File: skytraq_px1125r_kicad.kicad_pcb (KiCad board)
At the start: 2 copper layers, 35.5 x 27.6 mm, 11 parts, among them J1 Conn_01x04, J2 SMA, J3 SH_Conn_01x04, J4 Conn_01x04, U1 Skytraq_PX1125R

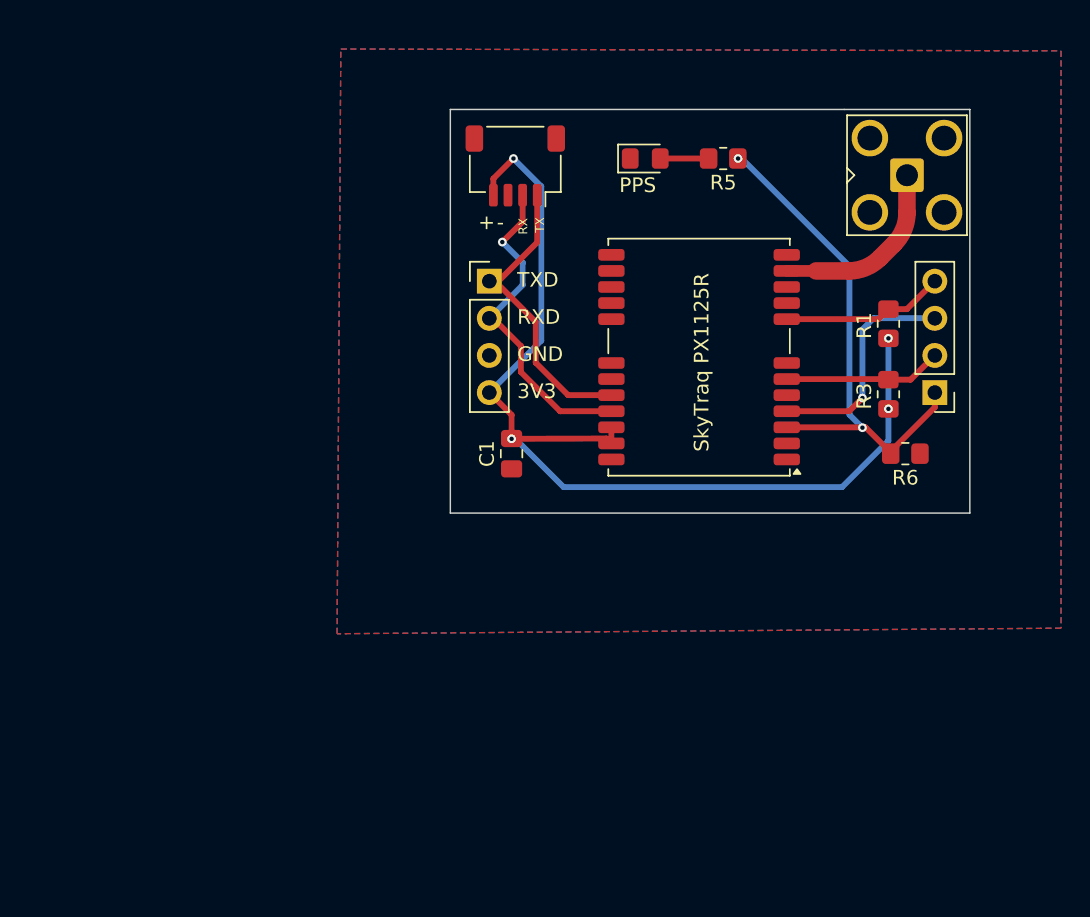
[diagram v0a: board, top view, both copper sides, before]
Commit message: 36x36 flight controller board
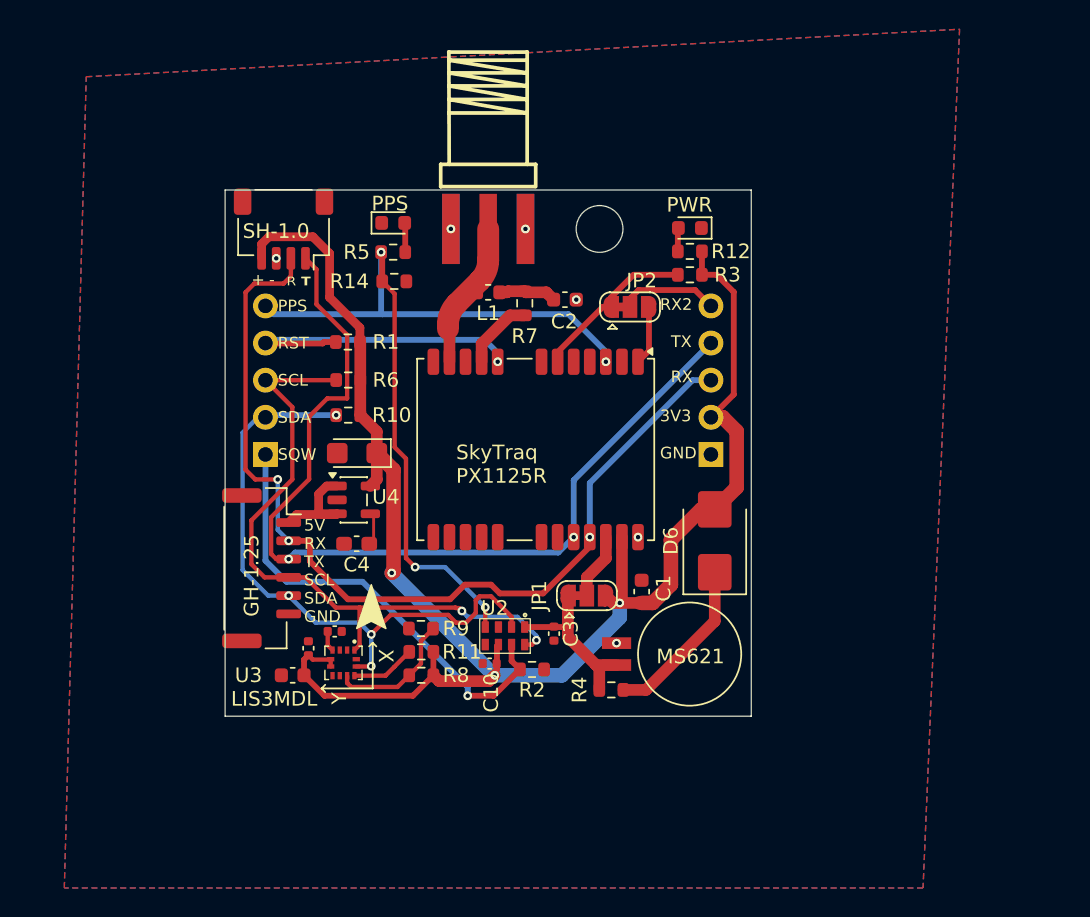
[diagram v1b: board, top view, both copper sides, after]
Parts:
- removed J3: SH_Conn_01x04, Connector_JST:JST_SH_SM04B-SRSS-TB_1x04-1MP_P1.00mm_Horizontal
- added BT1: MS621FE, Battery:BatteryHolder_Seiko_MS621F, F.Cu at (116.8, 71.8)
- added C10: 100nF, Capacitor_SMD:C_0402_1005Metric, F.Cu at (108.1, 72.4)
- added C2: 47pF, Capacitor_SMD:C_0603_1608Metric, F.Cu at (113.2, 47.5)
- added C23: 10uF, Capacitor_SMD:C_0603_1608Metric, F.Cu at (94.6, 73.2)
- added C3: 100nF, Capacitor_SMD:C_0402_1005Metric, F.Cu at (112.5, 70.3)
- added C4: 470pF, Capacitor_SMD:C_0603_1608Metric_Pad1.08x0.95mm_HandSolder, F.Cu at (99.0, 64.2)
- added C5: 2.2uF, Capacitor_Tantalum_SMD:CP_EIA-3216-18_Kemet-A, F.Cu at (99.0, 58.0)
- added C8: 100nF, Capacitor_SMD:C_0402_1005Metric, F.Cu at (95.7, 71.4)
- added C9: 100nF, Capacitor_SMD:C_0402_1005Metric, F.Cu at (97.5, 70.2)
- added D1: BLUE, LED_SMD:LED_0603_1608Metric, F.Cu at (121.8, 42.6)
- added D6: D_Schottky, Diode_SMD:D_SMB, F.Cu at (123.5, 64.0)
- added H1: MountingHole, MountingHole:MountingHole_3.2mm_M3, F.Cu at (115.6, 42.7)
- added J5: Conn_01x05, Connector_PinHeader_2.54mm:PinHeader_1x05_P2.54mm_Horizontal, B.Cu at (92.8, 58.1)
- added J7: Conn_01x05, Connector_PinHeader_2.54mm:PinHeader_1x05_P2.54mm_Horizontal, B.Cu at (123.2, 58.1)
- added JP1: SolderJumper_3_Bridged12, Jumper:SolderJumper-3_P1.3mm_Bridged12_RoundedPad1.0x1.5mm, F.Cu at (114.8, 67.8)
- added JP2: SolderJumper_3_Bridged12, Jumper:SolderJumper-3_P1.3mm_Bridged12_RoundedPad1.0x1.5mm, F.Cu at (117.7, 48.0)
- added L1: 27nH, Inductor_SMD:L_0603_1608Metric, F.Cu at (108.0, 47.0)
- added R10: 10k, Resistor_SMD:R_0603_1608Metric, F.Cu at (98.4, 55.4)
- added R11: 10k, Resistor_SMD:R_0603_1608Metric, F.Cu at (103.4, 71.6)
- added R12: 1k, Resistor_SMD:R_0603_1608Metric, F.Cu at (121.8, 44.2)
- added R14: 10k, Resistor_SMD:R_0603_1608Metric, F.Cu at (101.6, 46.2)
- added R2: 10k, Resistor_SMD:R_0603_1608Metric, F.Cu at (111.0, 72.8)
- added R4: 1k, Resistor_SMD:R_0603_1608Metric, F.Cu at (116.4, 74.2)
- added R7: 10, Resistor_SMD:R_0603_1608Metric, F.Cu at (110.5, 47.8)
- added R8: 0, Resistor_SMD:R_0603_1608Metric, F.Cu at (103.4, 73.2)
- added R9: 0, Resistor_SMD:R_0603_1608Metric, F.Cu at (103.4, 70.0)
- added U2: RV-3032, MyFootprints:RV-3032, F.Cu at (109.2, 70.5)
- added U3: LIS3MDL, footprint_JLCPCB:LGA-12_L2.0-W2.0-P0.50-BL, F.Cu at (98.1, 72.4)
- added U4: MIC5219-3.3YM5, Package_TO_SOT_SMD:SOT-23-5, F.Cu at (98.8, 61.2)
- C1: footprint Capacitor_SMD:C_0805_2012Metric_Pad1.18x1.45mm_HandSolder -> Capacitor_SMD:C_0603_1608Metric
- D2: footprint LED_SMD:LED_0805_2012Metric_Pad1.15x1.40mm_HandSolder -> LED_SMD:LED_0603_1608Metric
- J1: value Conn_01x04 -> JST_GH_1.25_6P; footprint Connector_PinHeader_2.54mm:PinHeader_1x04_P2.54mm_Vertical -> Connector_JST:JST_GH_SM06B-GHS-TB_1x06-1MP_P1.25mm_Horizontal
- J2: footprint Connector_Coaxial:SMA_Amphenol_901-143_Horizontal -> footprint_JLCPCB:SMA-SMD_BWSMA-KE-P001
- J4: value Conn_01x04 -> JST_SH_1.00_4P; footprint Connector_PinHeader_2.54mm:PinHeader_1x04_P2.54mm_Vertical -> Connector_JST:JST_SH_SM04B-SRSS-TB_1x04-1MP_P1.00mm_Horizontal
- R1, R3, R6: footprint Resistor_SMD:R_0805_2012Metric_Pad1.20x1.40mm_HandSolder -> Resistor_SMD:R_0603_1608Metric
- R5: value 3k3 -> 1k; footprint Resistor_SMD:R_0805_2012Metric_Pad1.20x1.40mm_HandSolder -> Resistor_SMD:R_0603_1608Metric
- moved J1 47.6 mm to (92.5, 65.9), turned to -90 degrees
- moved R6 38.4 mm to (98.4, 53.0)
- moved R1 37.0 mm to (98.4, 50.4), turned to 180 degrees
- moved J2 28.9 mm to (108.0, 42.7), turned to 90 degrees
- moved R5 23.5 mm to (101.5, 44.2), turned to 0 degrees
- moved D2 17.8 mm to (101.5, 42.2)
- moved R3 15.9 mm to (121.8, 45.8), turned to 0 degrees
- moved J4 14.5 mm to (94.0, 42.7), turned to 180 degrees
- moved C1 13.0 mm to (118.5, 67.5)
- moved U1 12.8 mm to (111.2, 57.8), turned to -90 degrees
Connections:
- C1 pad 1: GND -> +3V3
- C1 pad 2: +3V3 -> GND
- J1 pad 1: GPS_PPS -> /+5V
- J1 pad 2: GPS_RXD2 -> GPS_RX
- J1 pad 3: GPS_EXTINT -> GPS_TX
- J1 pad 4: GPS_RST -> SCL
- J4 pad 1: GPS_TXD -> GPS_TX
- J4 pad 2: GPS_RXD -> GPS_RX
- R1 pad 1: GPS_RST -> +3V3
- R1 pad 2: +3V3 -> GPS_RST
- R3 pad 1: GPS_RXD2 -> Net-(JP2-A)
- R6 pad 1: GND -> +3V3
- R6 pad 2: GPS_PPS -> SCL
- U1 pad 1: unconnected-(U1-BOOT_SEL-Pad1) -> Net-(JP2-B)
- U1 pad 20: GPS_TXD -> GPS_TX
- U1 pad 21: GPS_RXD -> GPS_RX
- U1 pad 22: +3V3 -> Net-(JP1-C)
- U1 pad 4: GPS_EXTINT -> unconnected-(U1-ODO-Pad4)
- U1 pad 6: GPS_RXD2 -> Net-(JP2-A)
- U1 pad 9: unconnected-(U1-SPI_CSN-Pad9) -> Net-(U1-SPI_CSN)
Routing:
- net GPS_RX: track 0.00 -> 64.5 mm, vias 0 -> 3
- net GPS_TX: track 0.00 -> 63.0 mm, vias 0 -> 2
- net +3V3: track 68.7 -> 113.9 mm, vias 4 -> 3
- net SCL: track 0.00 -> 45.2 mm, vias 0 -> 2
- net SDA: track 0.00 -> 43.0 mm, vias 0 -> 4
- net RTC_CLK: track 0.00 -> 31.5 mm, vias 0 -> 1
- net GPS_PPS: track 35.3 -> 59.4 mm, vias 2 -> 4
- net GPS_RXD: track 22.6 -> 0.00 mm, vias 1 -> 0
- net GPS_TXD: track 20.8 -> 0.00 mm
- net GPS_EXTINT: track 15.5 -> 0.00 mm, vias 1 -> 0
- net /VBAT: track 0.00 -> 11.7 mm
- net Net-(D6-K): track 0.00 -> 11.5 mm
- net Net-(JP2-A): track 0.00 -> 11.5 mm
- net GPS_RXD2: track 10.8 -> 0.00 mm
- net GPS_RST: track 11.2 -> 21.8 mm, vias 0 -> 1
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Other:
- board size 35.5 x 27.6 mm -> 36 x 36 mm
- board text added: "5V"
- board text added: "GH-1.25"
- board text added: "LIS3MDL"
- board text added: "MS621"
- board text added: "PWR"
- board text added: "R"
- board text added: "RX2"
- board text added: "SCL"
- board text added: "SDA"
- board text added: "SH-1.0"
- board text added: "SQW"
- board text added: "T"
- board text removed: "ODO"
- board text removed: "RXD"
- board text removed: "RXD2"
- board text removed: "TXD"

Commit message: with px1105 unfinished
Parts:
- removed C4: 470pF, Capacitor_SMD:C_0603_1608Metric_Pad1.08x0.95mm_HandSolder
- removed C5: 2.2uF, Capacitor_Tantalum_SMD:CP_EIA-3216-18_Kemet-A
- removed J4: JST_SH_1.00_4P, Connector_JST:JST_SH_SM04B-SRSS-TB_1x04-1MP_P1.00mm_Horizontal
- removed U4: MIC5219-3.3YM5, Package_TO_SOT_SMD:SOT-23-5
- added C6: 22uF, Capacitor_Tantalum_SMD:CP_EIA-3216-18_Kemet-A, F.Cu at (79.9, 62.1)
- added C7: 10uF, Capacitor_SMD:C_0603_1608Metric, F.Cu at (84.7, 61.8)
- added U5: ~, MyFootprints:skytraq_px1105, B.Cu at (111.2, 53.5)
- added U6: AMS1117-3.3, Package_TO_SOT_SMD:SOT-223-3_TabPin2, F.Cu at (81.9, 56.4)
- D6: footprint Diode_SMD:D_SMB -> Diode_SMD:D_SOD-323
- J2: footprint footprint_JLCPCB:SMA-SMD_BWSMA-KE-P001 -> footprint_JLCPCB:SMA-SMD_BWSMA-KE-P001_Symmetric
- J5: value Conn_01x05 -> Conn_01x04; footprint Connector_PinHeader_2.54mm:PinHeader_1x05_P2.54mm_Horizontal -> Connector_PinSocket_2.54mm:PinSocket_1x04_P2.54mm_Vertical
- J7: value Conn_01x05 -> Conn_01x06; footprint Connector_PinHeader_2.54mm:PinHeader_1x05_P2.54mm_Horizontal -> Connector_PinHeader_2.54mm:PinHeader_1x06_P2.54mm_Vertical
- moved J7 2.54 mm to (123.2, 60.6)
- moved D6 1.80 mm to (123.5, 65.8)
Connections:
- net Net-(J2-In) renamed /GPS_RF
- net Net-(JP1-C) renamed /GPS_V_BCKP
- net Net-(JP2-A) renamed /GPS_RX2
- net Net-(JP2-B) renamed /GPS_BOOT
- J7 pad 5: BOOT/GPS_RXD2 -> GPS_PPS
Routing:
- net GPS_TX: track 63.0 -> 40.0 mm, vias 2 -> 3
- net GPS_PPS: track 59.4 -> 78.7 mm, vias 4 -> 2
- net GPS_RX: track 64.5 -> 45.5 mm, vias 3 -> 1
- net GPS_RST: track 21.8 -> 33.8 mm
- net +3V3: track 113.9 -> 101.9 mm
- net /GPS_RX2: track 11.5 -> 21.8 mm, vias 0 -> 1
- net /GPS_V_BCKP: track 4.54 -> 13.5 mm, vias 0 -> 1
- net /+5V: track 7.58 -> 0.00 mm
- net /GPS_RF: track 10.1 -> 16.0 mm
- net /GPS_BOOT: track 4.06 -> 6.76 mm, vias 0 -> 2
- net Net-(U4-BP): track 2.10 -> 0.00 mm
- net Net-(D6-K): track 11.5 -> 10.8 mm
- net GND: vias 6 -> 4
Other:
- board text removed: "+"
- board text removed: "-"
- board text removed: "R"
- board text removed: "SH-1.0"
- board text removed: "T"

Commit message: px1105 4-layers boar
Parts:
- added C4: 100nF, Capacitor_SMD:C_0402_1005Metric, B.Cu at (110.7, 61.2)
- added C5: 10uF, Capacitor_SMD:C_0603_1608Metric, B.Cu at (107.2, 61.6)
- added J3: JST_GH_1.25_6P, Connector_JST:JST_GH_SM06B-GHS-TB_1x06-1MP_P1.25mm_Horizontal, B.Cu at (120.2, 73.2)
- J5: value Conn_01x04 -> Conn_01x06; footprint Connector_PinSocket_2.54mm:PinSocket_1x04_P2.54mm_Vertical -> Connector_PinHeader_2.54mm:PinHeader_1x06_P2.54mm_Vertical
- U6: footprint Package_TO_SOT_SMD:SOT-223-3_TabPin2 -> Package_TO_SOT_SMD:SOT-89-3
- moved C6 20.2 mm to (98.8, 54.8)
- moved U6 17.0 mm to (98.8, 58.5), turned to 90 degrees
- moved C7 14.8 mm to (99.5, 62.5)
- moved R10 2.70 mm to (97.9, 52.8)
- moved J1 2.54 mm to (92.5, 68.4)
- moved J5 2.54 mm to (92.8, 60.6)
- moved R6 2.04 mm to (98.0, 51.0)
- moved R1 1.94 mm to (98.0, 48.5)
- moved C23 1.79 mm to (96.4, 73.4)
- moved R11 1.76 mm to (105.2, 71.8)
- moved R9 1.76 mm to (105.2, 70.2)
- moved C8 1.76 mm to (97.5, 71.5)
- moved C9 1.76 mm to (99.3, 70.3)
- moved R8 1.76 mm to (105.2, 73.3)
- moved U3 1.76 mm to (99.9, 72.5)
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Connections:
- J1 pad MP: GND -> unconnected-(J1-MountPin-PadMP)
- J5 pad 1: RTC_CLK -> /+5V
- J5 pad 2: SDA -> GND
- J5 pad 3: SCL -> RTC_CLK
- J5 pad 4: GPS_RST -> SDA
- J7 pad 1: GND -> +3V3
- J7 pad 2: +3V3 -> GND
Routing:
- net /+5V: track 0.00 -> 56.1 mm, vias 0 -> 3
- net BOOT/GPS_RXD2: track 6.81 -> 32.3 mm
- net GPS_RST: track 33.8 -> 59.3 mm, vias 1 -> 2
- net RTC_CLK: track 31.5 -> 44.1 mm
- net +3V3: track 101.9 -> 110.8 mm, vias 3 -> 14
- net GPS_PPS: track 78.7 -> 87.0 mm
- net SDA: track 43.0 -> 49.1 mm
- net GPS_TX: track 40.0 -> 45.6 mm, vias 3 -> 1
- net /GPS_V_BCKP: track 13.5 -> 16.3 mm, vias 1 -> 3
- net SCL: track 45.2 -> 47.5 mm
- net GPS_RX: track 45.5 -> 43.7 mm
- net GND: track 0.00 -> 1.60 mm, vias 4 -> 42
- net /VBAT: track 11.7 -> 10.8 mm
- added copper zone on In1.Cu, net GND
- added copper zone on In2.Cu, net GND
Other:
- copper layers 2 -> 4
- board text added: "RV3032"
- board text added: "SkyTraq PX1105"
- board text added: "SkyTraq PX1125"
- board text added: "V0.1"
- board text removed: "SkyTraq PX1125R"

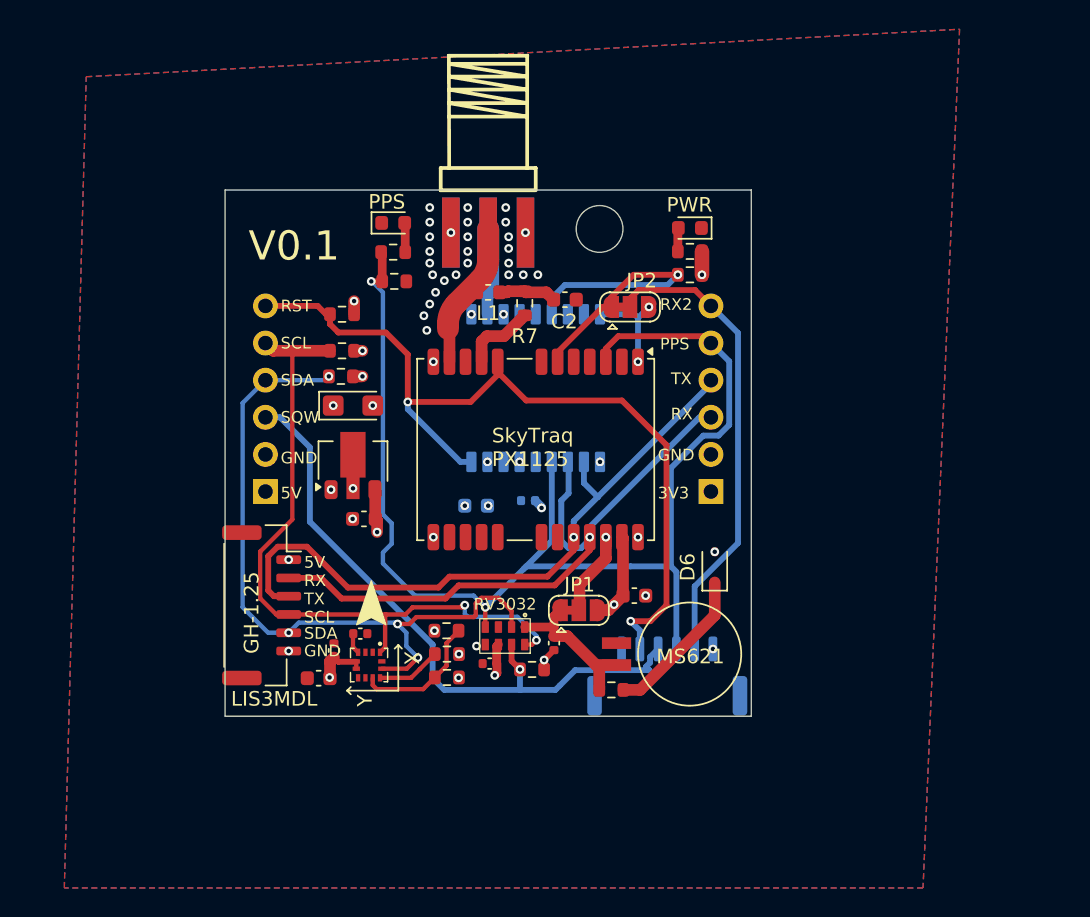
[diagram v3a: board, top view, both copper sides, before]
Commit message: added 2 M3 mounting holes
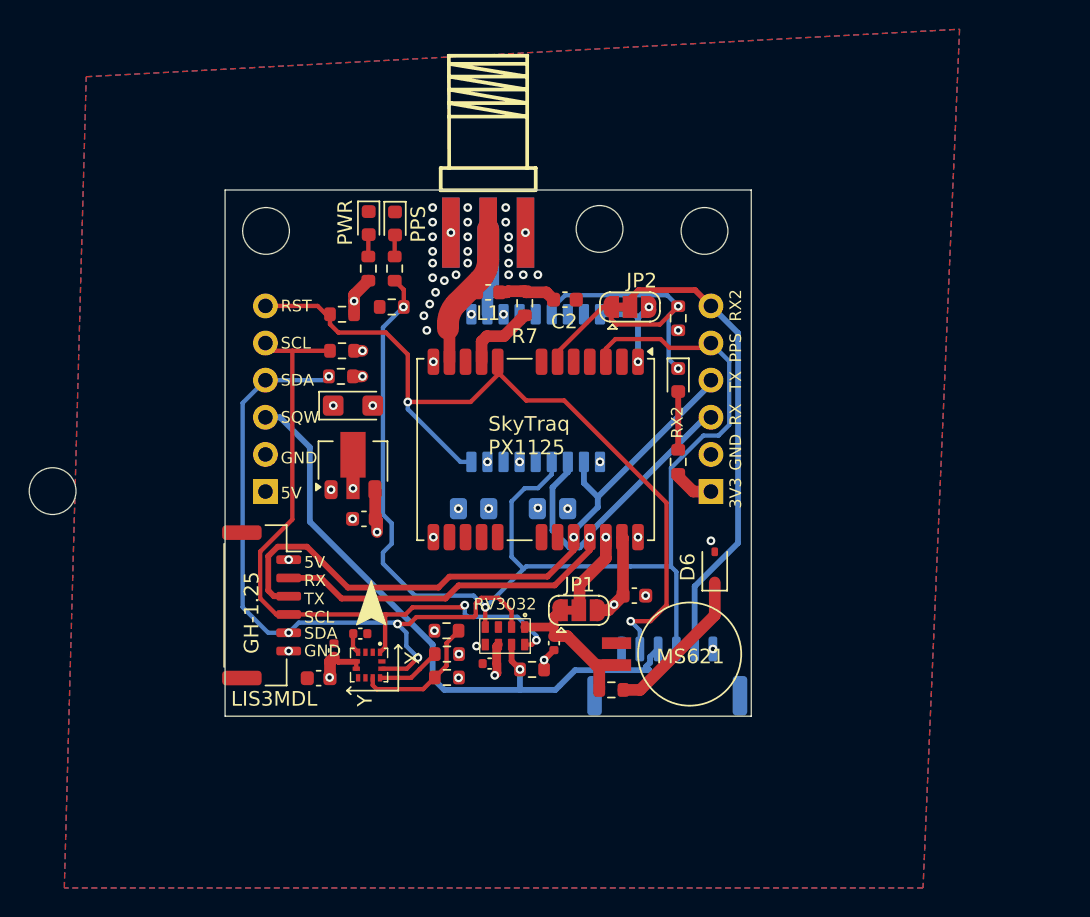
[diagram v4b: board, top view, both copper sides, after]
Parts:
- added D3: GREEN, LED_SMD:LED_0603_1608Metric, F.Cu at (121.0, 53.0)
- added H2: MountingHole, MountingHole:MountingHole_3.2mm_M3, F.Cu at (92.8, 42.8)
- added H3: MountingHole, MountingHole:MountingHole_3.2mm_M3, F.Cu at (122.8, 42.8)
- added H4: MountingHole, MountingHole:MountingHole_3.2mm_M3, F.Cu at (78.2, 60.6)
- added R13: 1k, Resistor_SMD:R_0603_1608Metric, F.Cu at (121.0, 58.6)
- C4: footprint Capacitor_SMD:C_0402_1005Metric -> Capacitor_SMD:C_0805_2012Metric_Pad1.18x1.45mm_HandSolder
- C5: footprint Capacitor_SMD:C_0603_1608Metric -> Capacitor_SMD:C_0805_2012Metric_Pad1.18x1.45mm_HandSolder
- J2: footprint footprint_JLCPCB:SMA-SMD_BWSMA-KE-P001_Symmetric -> footprint:SMA-SMD_BWSMA-KE-P001_Symmetric
- U3: footprint footprint_JLCPCB:LGA-12_L2.0-W2.0-P0.50-BL -> footprint:LGA-12_L2.0-W2.0-P0.50-BL
- moved R12 22.0 mm to (99.8, 45.4), turned to 90 degrees
- moved D1 22.0 mm to (99.8, 42.3), turned to -90 degrees
- moved R3 3.08 mm to (121.0, 48.8), turned to -90 degrees
- moved R14 1.76 mm to (101.4, 48.0), turned to 180 degrees
- moved C4 1.76 mm to (112.4, 61.8), turned to 0 degrees
- moved R5 1.13 mm to (101.6, 45.4), turned to 90 degrees
- moved C5 0.27 mm to (107.0, 61.8)
- moved D2 0.13 mm to (101.6, 42.3), turned to -90 degrees
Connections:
- net BOOT/GPS_RXD2 renamed BOOT/GPS_RX2
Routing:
- net /GPS_RX2: track 21.8 -> 26.2 mm, vias 1 -> 2
- net Net-(D3-A): track 0.00 -> 3.99 mm
- net GPS_RST: track 59.3 -> 56.9 mm
- net /GPS_V_BCKP: track 16.3 -> 18.6 mm
- net +3V3: track 110.8 -> 113.1 mm
- net GPS_PPS: track 87.0 -> 86.1 mm
- net Net-(D2-A): track 2.02 -> 1.49 mm
- net GND: vias 42 -> 43
